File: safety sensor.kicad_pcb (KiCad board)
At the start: 2 copper layers, 99.1 x 45.7 mm, 29 parts, among them IC1 STM8S003F3P6, J1 Conn_01x02, J2 SDA, J3 SCL, J4 INT, J5 Conn_01x02, J6 SWIM, U1 LD1117V33, U2 VCNL3020-GS08

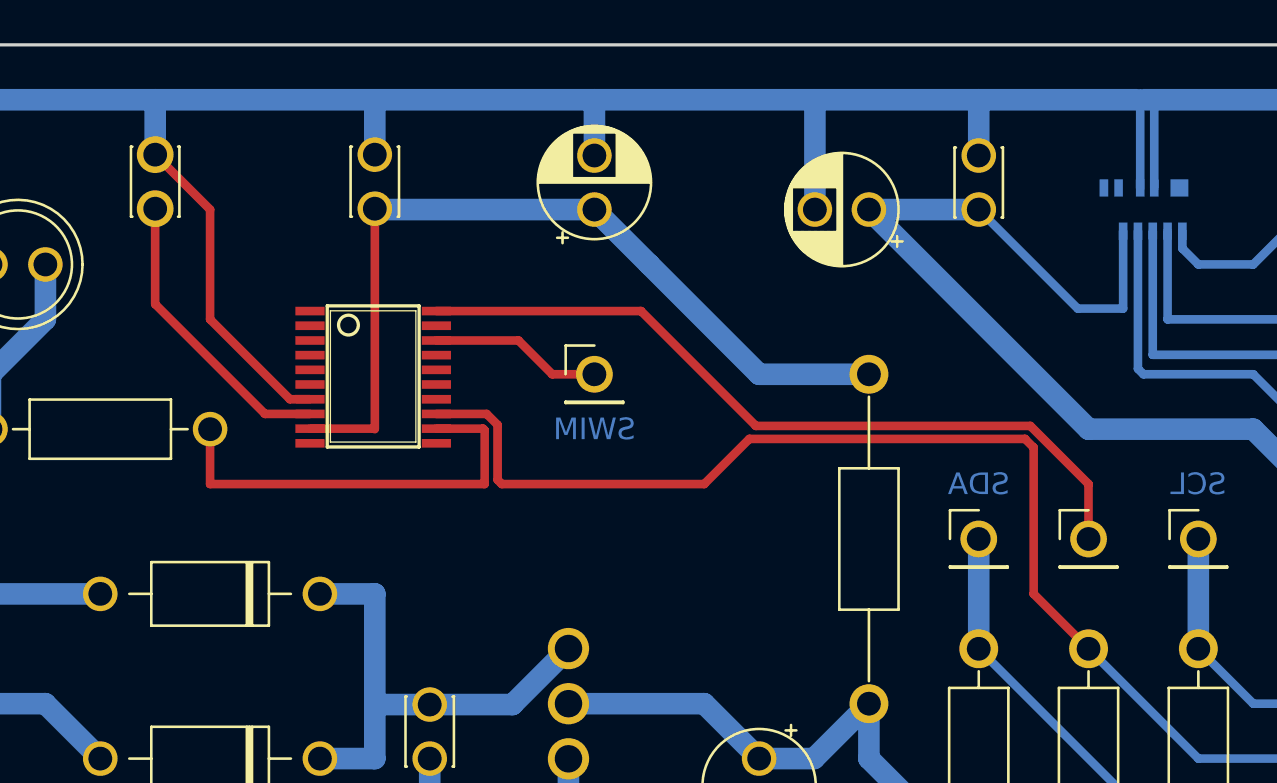
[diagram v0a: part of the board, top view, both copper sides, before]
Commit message: flip stm8 side
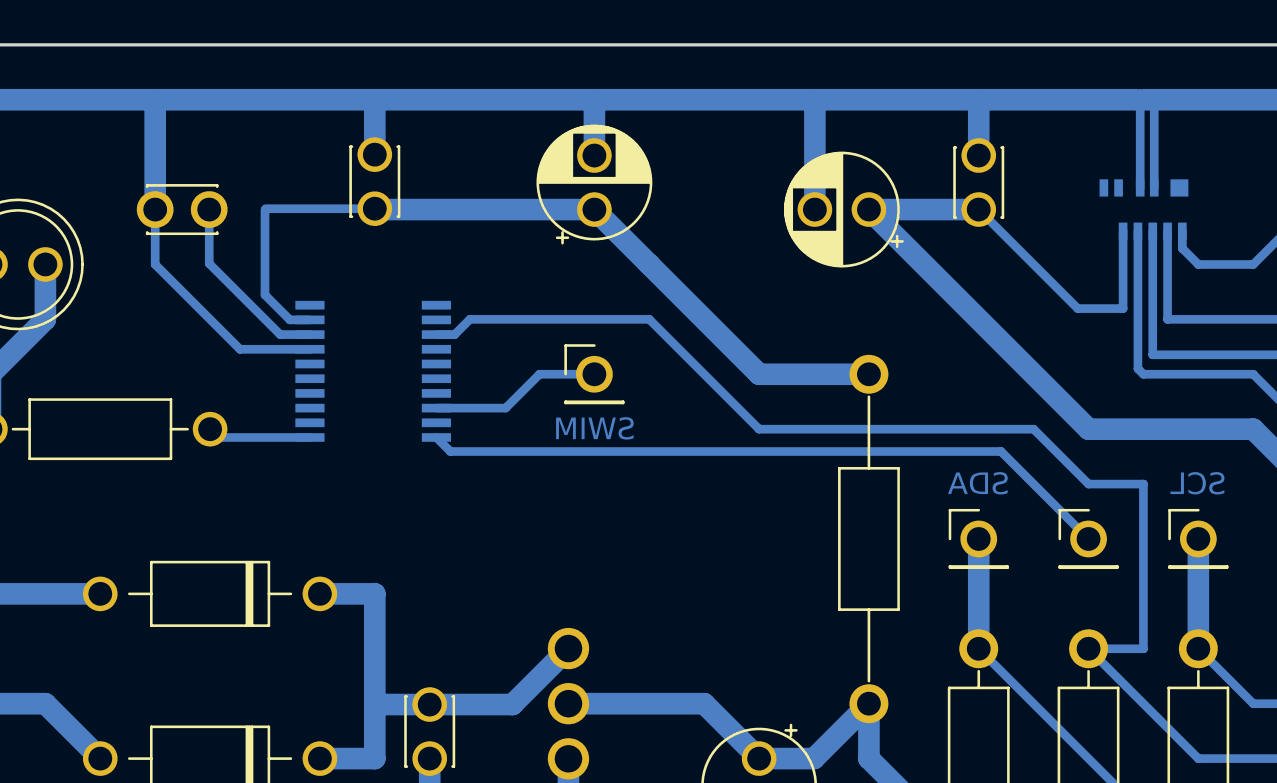
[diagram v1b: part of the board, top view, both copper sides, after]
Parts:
- IC1: moved to B.Cu
- moved C3 2.54 mm to (38.1, 25.4), turned to 0 degrees
- turned IC1 to 90 degrees
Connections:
- IC1 pad 1: unconnected-(IC1-Pad1) -> Net-(IC1-Pad1)
- IC1 pad 12: Net-(IC1-Pad12) -> unconnected-(IC1-Pad12)
- R7 pad 2: Net-(IC1-Pad12) -> Net-(IC1-Pad1)
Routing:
- net Net-(IC1-Pad12): track 20.0 -> 0.00 mm
- net Net-(C3-Pad2): track 13.7 -> 8.52 mm
- net Net-(IC1-Pad1): track 0.00 -> 4.78 mm
- net Net-(IC1-Pad13): track 89.5 -> 93.9 mm
- net Net-(IC1-Pad20): track 36.0 -> 32.1 mm
- net +3.3V: track 139.2 -> 137.5 mm
- net GND: track 330.0 -> 328.4 mm

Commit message: add pull up resistor for nrst, change hole size for voltage connectors
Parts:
- added R8: 10K, Resistor_THT:R_Axial_DIN0207_L6.3mm_D2.5mm_P10.16mm_Horizontal, F.Cu at (58.4, 40.6)
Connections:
- IC1 pad 4: unconnected-(IC1-Pad4) -> Net-(IC1-Pad4)
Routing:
- net +3.3V: track 137.5 -> 153.4 mm
- net Net-(IC1-Pad4): track 0.00 -> 9.73 mm
